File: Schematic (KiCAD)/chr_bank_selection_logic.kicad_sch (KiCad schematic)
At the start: 40 parts

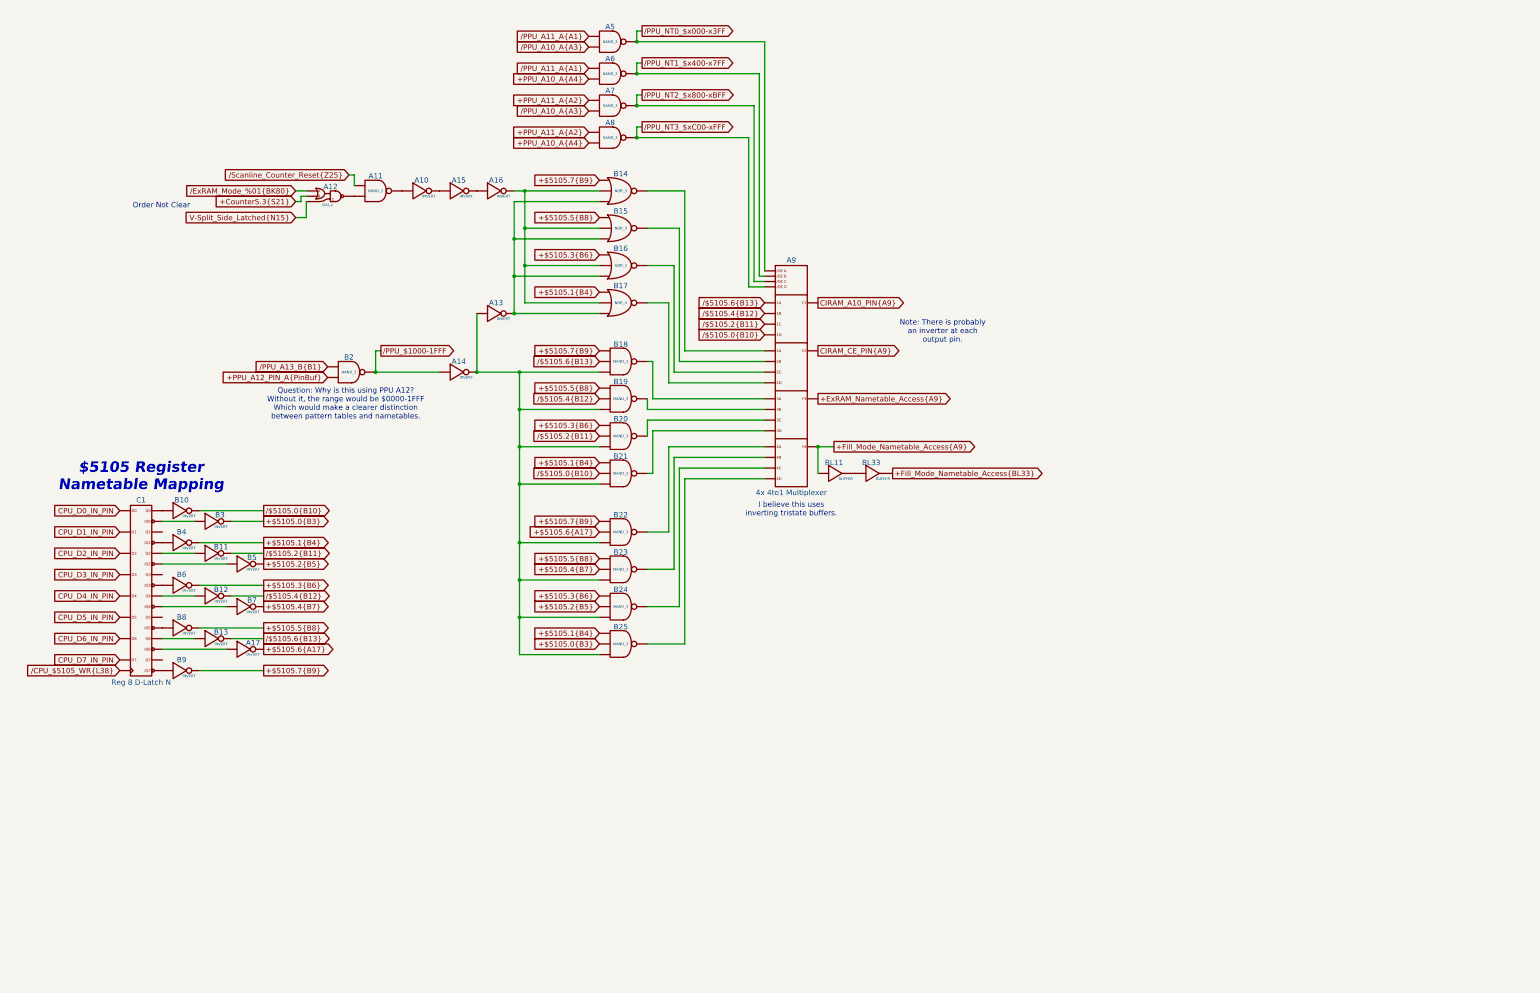
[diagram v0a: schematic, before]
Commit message: Schematic Updates:  - Added all 10-bit CHR banking registers $5120 - $512B, including where all 10 bits come from when written.  - Added 8-bit CHR bank register $5202, which is the bank used when rendering the V-Split region.    + V-Split seems to always be 8-bit, 8kB bank regardless of CHR mode.  The wiki doesn't say that and I don't know for sure.  - Added decoding logic that activates the correct CHR bank for CHR A10, A11, A12 (corresponding to columns AV, AW, AX).  - Noted, AX15 activates $5202 CHR Bank for V-Split region.  AX16 activates CHR Bank from data stored in ExRAM for extended attributes.  Therefore, AX15 driven by AT1 High means we specifically are in v-split region, and not extended attribute mode.  With this knowledge, backtracking up the chain from AT1 to N14 sheds very useful insight what the 3-bit shift register at N11/N12/N13 is doing.  We now know that N14 goes low specifically for pattern table fetches when rendering the V-split region, and does not appear dual-purposed for extended attribute fetch sequencing.  This may seem rather subtle or unimportant, but it is a good advancement for higher level understanding what that mysterious shift register might be doing.
SVG Trace Updates:
 - Registers $5120, 5121, 5122, 5123 (first 4 CHR bank register), the outputs were labeled in reverse order.
 - Register $5130 (highest CHR bank bits), the outputs were labeled with backwards polarity.  The error was not having taken into account that the CPU data bus input to the latches came already inverted to begin with.
 - Still wrong: Cell AV7, 2-input NAND gate.  One of the inputs is missing and it logically should be driven by AS19 like the 4 cells to its direct right.  I can't quite make out how it makes that connection.
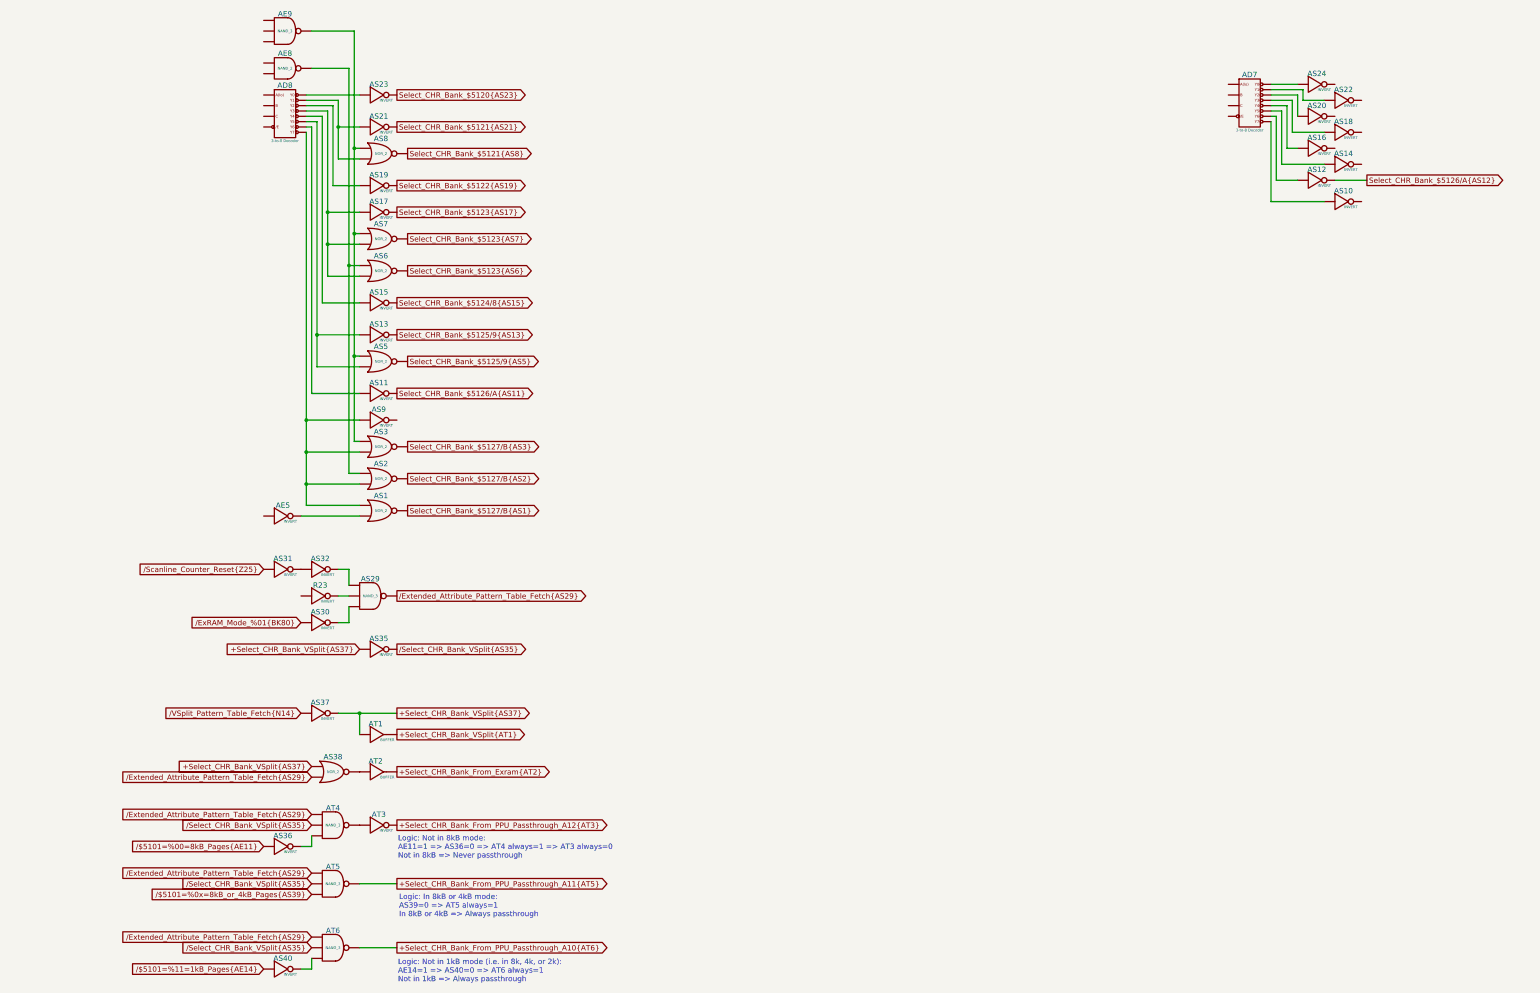
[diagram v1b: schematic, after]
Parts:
- removed A10, A13, A14, A15, A16, A17, B10, B11, B12, B13, B3, B4, B5, B6, B7, B8, B9: INVERT, symbol MMC5:INVERT
- removed A11, A5, A6, A7, A8, B2: NAND_2, symbol MMC5:NAND_2
- removed A12: OAI_2, symbol MMC5:OAI_2
- removed A9: 4x 4to1 Multiplexer, symbol MMC5:Multiplexer_4x4to1
- removed B14, B15, B16, B17: NOR_3, symbol MMC5:NOR_3
- removed B18, B19, B20, B21, B22, B23, B24, B25: NAND_3, symbol MMC5:NAND_3
- removed BL11, BL33: BUFFER, symbol MMC5:BUFFER
- removed C1: Reg 8 D-Latch N, symbol MMC5:Reg_8_D-Latch_N
- added AD7, AD8: 3-to-8 Decoder, symbol MMC5:Decoder_3to8
- added AE5, AS10, AS11, AS12, AS13, AS14, AS15, AS16, AS17, AS18, AS19, AS20, AS21, AS22, AS23, AS24, AS30, AS31, AS32, AS35, AS36, AS37, AS40, AS9, AT3, R23: INVERT, symbol MMC5:INVERT
- added AE8: NAND_2, symbol MMC5:NAND_2
- added AE9, AS29, AT4, AT5, AT6: NAND_3, symbol MMC5:NAND_3
- added AS1, AS2, AS3, AS38, AS5, AS6, AS7, AS8: NOR_2, symbol MMC5:NOR_2
- added AT1, AT2: BUFFER, symbol MMC5:BUFFER
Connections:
- net /ExRAM_Mode_%01{BK80}: now also AS30. (X)
- net /Scanline_Counter_Reset{Z25}: now also AS31. (X)
- new net: AE5. (X), AS1. (X)
- new net: AS29. (X), R23. (X)
- new net: AE9. (X), AS3. (X), AS5. (X), AS7. (X), AS8. (X)
- new net: AD8. (/Y7), AS1. (X), AS2. (X), AS3. (X), AS9. (X)
- new net: AS29. (X), AS32. (X)
- new net: AS29. (X), AS30. (X)
- new net: AT3. (X), AT4. (X)
- new net: AS40. (X), AT6. (X)
- new net: AD8. (/Y7), AS21. (X), AS8. (X)
- new net: AD7. (/Y7), AS14. (X)
- new net: AD7. (/Y7), AS18. (X)
- new net: AD8. (/Y7), AS17. (X), AS6. (X), AS7. (X)
- new net: AD8. (/Y7), AS23. (X)
- new net: AS38. (X), AT2. (X)
- new net: AS36. (X), AT4. (X)
- new net: AD7. (/Y7), AS20. (X)
- new net: AD7. (/Y7), AS12. (X)
- new net: AD8. (/Y7), AS13. (X), AS5. (X)
- new net: AD8. (/Y7), AS11. (X)
- new net: AE8. (X), AS2. (X), AS6. (X)
- new net: AS31. (X), AS32. (X)
- new net: AD8. (/Y7), AS15. (X)
- new net: AD8. (/Y7), AS19. (X)
- new net: AD7. (/Y7), AS10. (X)
- new net: AD7. (/Y7), AS22. (X)
- new net: AD7. (/Y7), AS24. (X)
- new net: AD7. (/Y7), AS16. (X)
- new net +Select_CHR_Bank_From_Exram{AT2}: AT2. (X)
- new net +Select_CHR_Bank_From_PPU_Passthrough_A10{AT6}: AT6. (X)
- new net +Select_CHR_Bank_From_PPU_Passthrough_A11{AT5}: AT5. (X)
- new net +Select_CHR_Bank_From_PPU_Passthrough_A12{AT3}: AT3. (X)
- new net +Select_CHR_Bank_VSplit{AS37}: AS35. (X), AS37. (X), AS38. (X), AT1. (X)
- new net +Select_CHR_Bank_VSplit{AT1}: AT1. (X)
- new net Select_CHR_Bank_$5120{AS23}: AS23. (X)
- new net Select_CHR_Bank_$5121{AS21}: AS21. (X)
- new net Select_CHR_Bank_$5121{AS8}: AS8. (X)
- new net Select_CHR_Bank_$5122{AS19}: AS19. (X)
- new net Select_CHR_Bank_$5123{AS17}: AS17. (X)
- new net Select_CHR_Bank_$5123{AS6}: AS6. (X)
- new net Select_CHR_Bank_$5123{AS7}: AS7. (X)
- new net Select_CHR_Bank_$5124/8{AS15}: AS15. (X)
- new net Select_CHR_Bank_$5125/9{AS13}: AS13. (X)
- new net Select_CHR_Bank_$5125/9{AS5}: AS5. (X)
- new net Select_CHR_Bank_$5126/A{AS11}: AS11. (X)
- new net Select_CHR_Bank_$5126/A{AS12}: AS12. (X)
- new net Select_CHR_Bank_$5127/B{AS1}: AS1. (X)
- new net Select_CHR_Bank_$5127/B{AS2}: AS2. (X)
- new net Select_CHR_Bank_$5127/B{AS3}: AS3. (X)
- new net /$5101=%00=8kB_Pages{AE11}: AS36. (X)
- new net /$5101=%0x=8kB_or_4kB_Pages{AS39}: AT5. (X)
- new net /$5101=%11=1kB_Pages{AE14}: AS40. (X)
- new net /Extended_Attribute_Pattern_Table_Fetch{AS29}: AS29. (X), AS38. (X), AT4. (X), AT5. (X), AT6. (X)
- new net /Select_CHR_Bank_VSplit{AS35}: AS35. (X), AT4. (X), AT5. (X), AT6. (X)
- new net /VSplit_Pattern_Table_Fetch{N14}: AS37. (X)
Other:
- note added: "Logic: In 8kB or 4kB mode: AS39=0 => AT5 always=1 In 8kB or 4kB => Always passthrough"
- note added: "Logic: Not in 1kB mode (i.e. in 8k, 4k, or 2k): AE14=1 => AS40=0 => AT6 always=1 Not in 1kB => Always passthrough"
- note added: "Logic: Not in 8kB mode: AE11=1 => AS36=0 => AT4 always=1 => AT3 always=0 Not in 8kB => Never passthrough"
- note removed: "$5105 Register Nametable Mapping"
- note removed: "I believe this uses inverting tristate buffers."
- note removed: "Note: There is probably an inverter at each output pin."
- note removed: "Order Not Clear"
- note removed: "Question: Why is this using PPU A12? Without it, the range would be $0000-1FFF Which would make a clearer distinction between pattern tables and nametables."

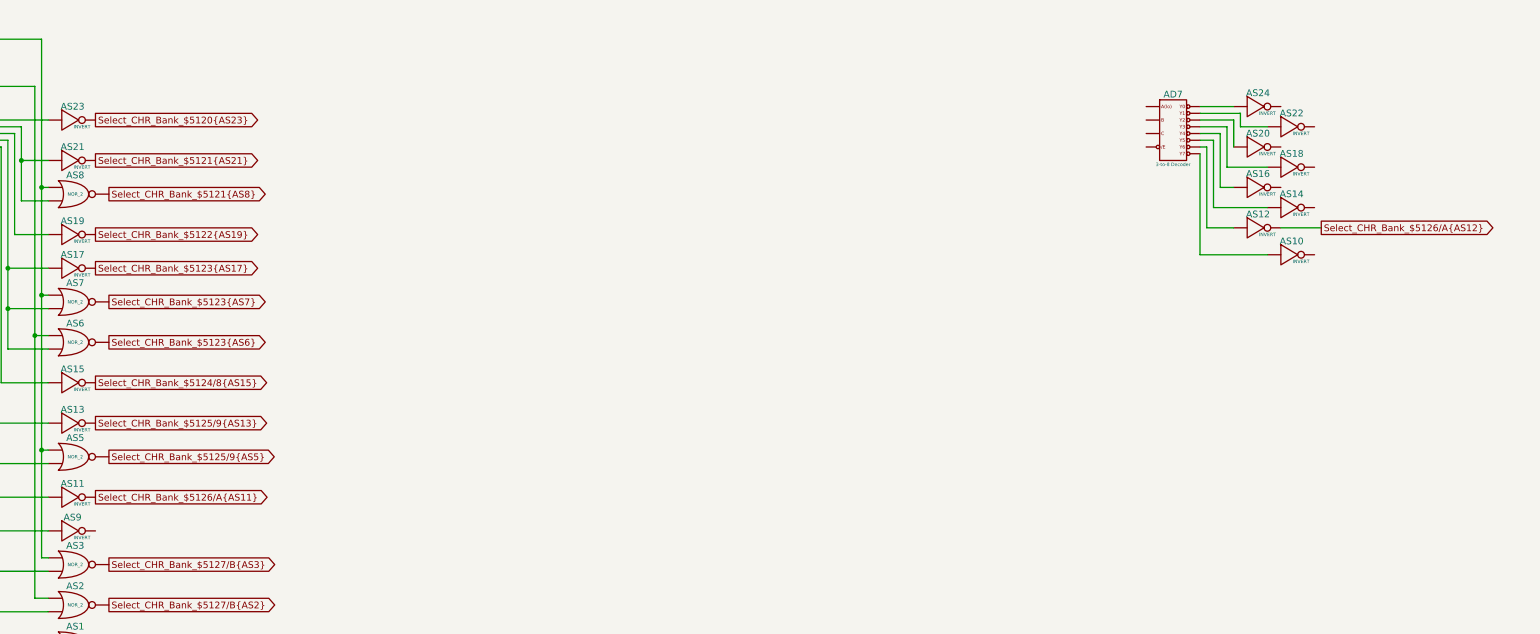
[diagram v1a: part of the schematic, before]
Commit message: - Finished up the CHR Ax bits.
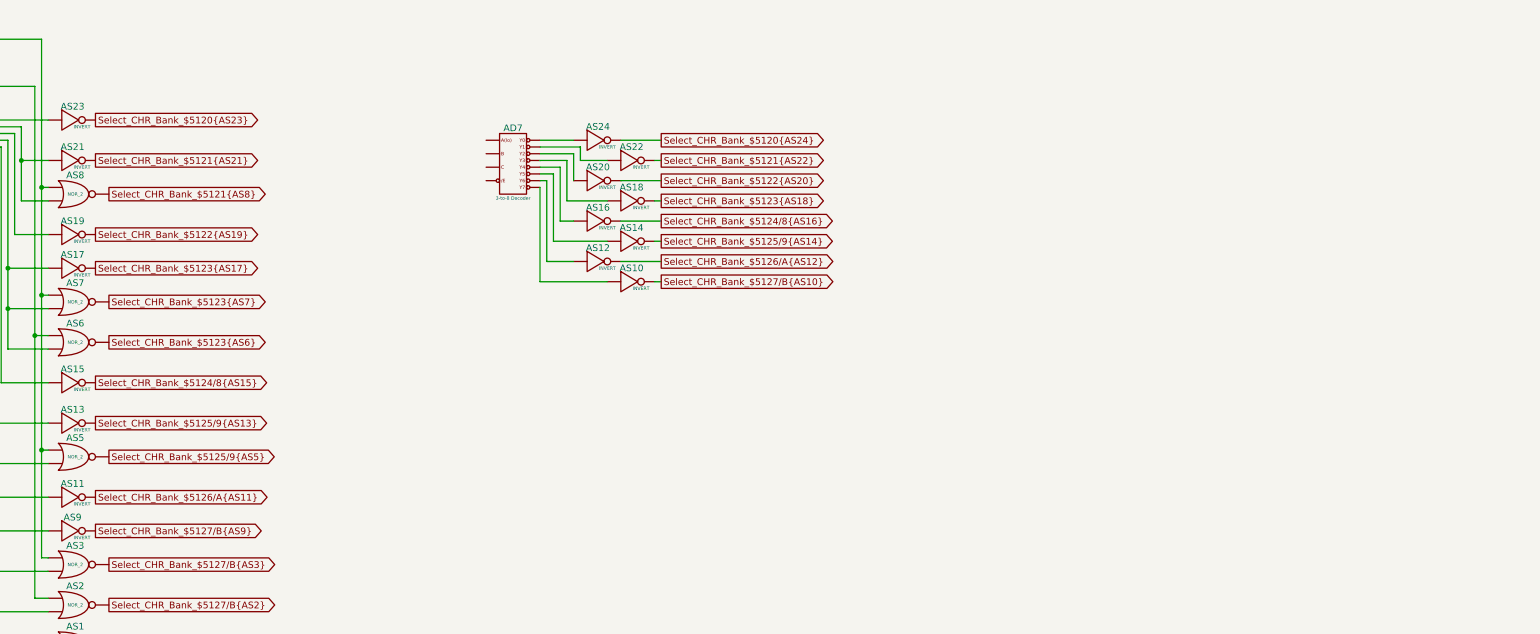
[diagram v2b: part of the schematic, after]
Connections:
- net at AE5. (X): now also AS1. (X)
- net at R23. (X): now also AS29. (X)
- net at AS32. (X): now also AS31. (X); no longer AS29. (X)
- net Select_CHR_Bank_$5125/9{AS14}: now reaches AS14. (X)
- net at AD7. (/Y7): now also AS16. (X); no longer AS14. (X)
- net Select_CHR_Bank_$5123{AS18}: now reaches AS18. (X)
- net at AD8. (/Y7): now also AS19. (X); no longer AS23. (X)
- net Select_CHR_Bank_$5122{AS20}: now reaches AS20. (X)
- net at AE8. (X): now also AS2. (X), AS6. (X)
- net Select_CHR_Bank_$5127/B{AS9}: now reaches AS9. (X)
- net Select_CHR_Bank_$5127/B{AS10}: now reaches AS10. (X)
- net Select_CHR_Bank_$5121{AS22}: now reaches AS22. (X)
- net Select_CHR_Bank_$5120{AS24}: now reaches AS24. (X)
- net Select_CHR_Bank_$5120{AS24}: no longer AD7. (/Y7)
- net Select_CHR_Bank_$5124/8{AS16}: now reaches AS16. (X)
- net Select_CHR_Bank_$5124/8{AS16}: no longer AD7. (/Y7)
- new net: AE9. (X), AS3. (X), AS5. (X), AS7. (X), AS8. (X)
- new net: AD8. (/Y7), AS1. (X), AS2. (X), AS3. (X), AS9. (X)
- new net: AS29. (X), AS32. (X)
- new net: AS29. (X), AS30. (X)
- new net: AT3. (X), AT4. (X)
- new net: AS40. (X), AT6. (X)
- new net: AD8. (/Y7), AS21. (X), AS8. (X)
- new net: AD7. (/Y7), AS14. (X)
- new net: AD7. (/Y7), AS18. (X)
- new net: AD8. (/Y7), AS17. (X), AS6. (X), AS7. (X)
- new net: AD8. (/Y7), AS23. (X)
- new net: AS38. (X), AT2. (X)
- new net: AS36. (X), AT4. (X)
- new net: AD7. (/Y7), AS20. (X)
- new net: AD7. (/Y7), AS12. (X)
- new net: AD8. (/Y7), AS13. (X), AS5. (X)
- new net: AD8. (/Y7), AS11. (X)
- new net: AD8. (/Y7), AS15. (X)
- new net: AD7. (/Y7), AS10. (X)
- new net: AD7. (/Y7), AS22. (X)
- new net: AD7. (/Y7), AS24. (X)
- now unconnected: AE9. (X)
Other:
- moved on the sheet: AD7, AS10, AS12, AS14, AS16, AS18, AS20, AS22, AS24
